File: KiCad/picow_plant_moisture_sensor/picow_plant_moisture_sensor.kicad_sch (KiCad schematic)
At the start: 28 parts, among them J1 Conn_01x03, J10 Conn_01x03, J11 Conn_01x03, J12 Conn_01x03, J13 Conn_01x03, J14 ADS1115, J15 ADS1115, J16 ADS1115, J2 Conn_01x03, J3 Conn_01x03, J4 Conn_01x03, J5 Conn_01x03, J6 Conn_01x03, J7 Conn_02x03_Odd_Even, J8 Conn_01x03, J9 Conn_01x03, SW1 SW_Push, SW2 SW_Push, SW3 SW_Push, SW4 SW_Push, U2 PicoW

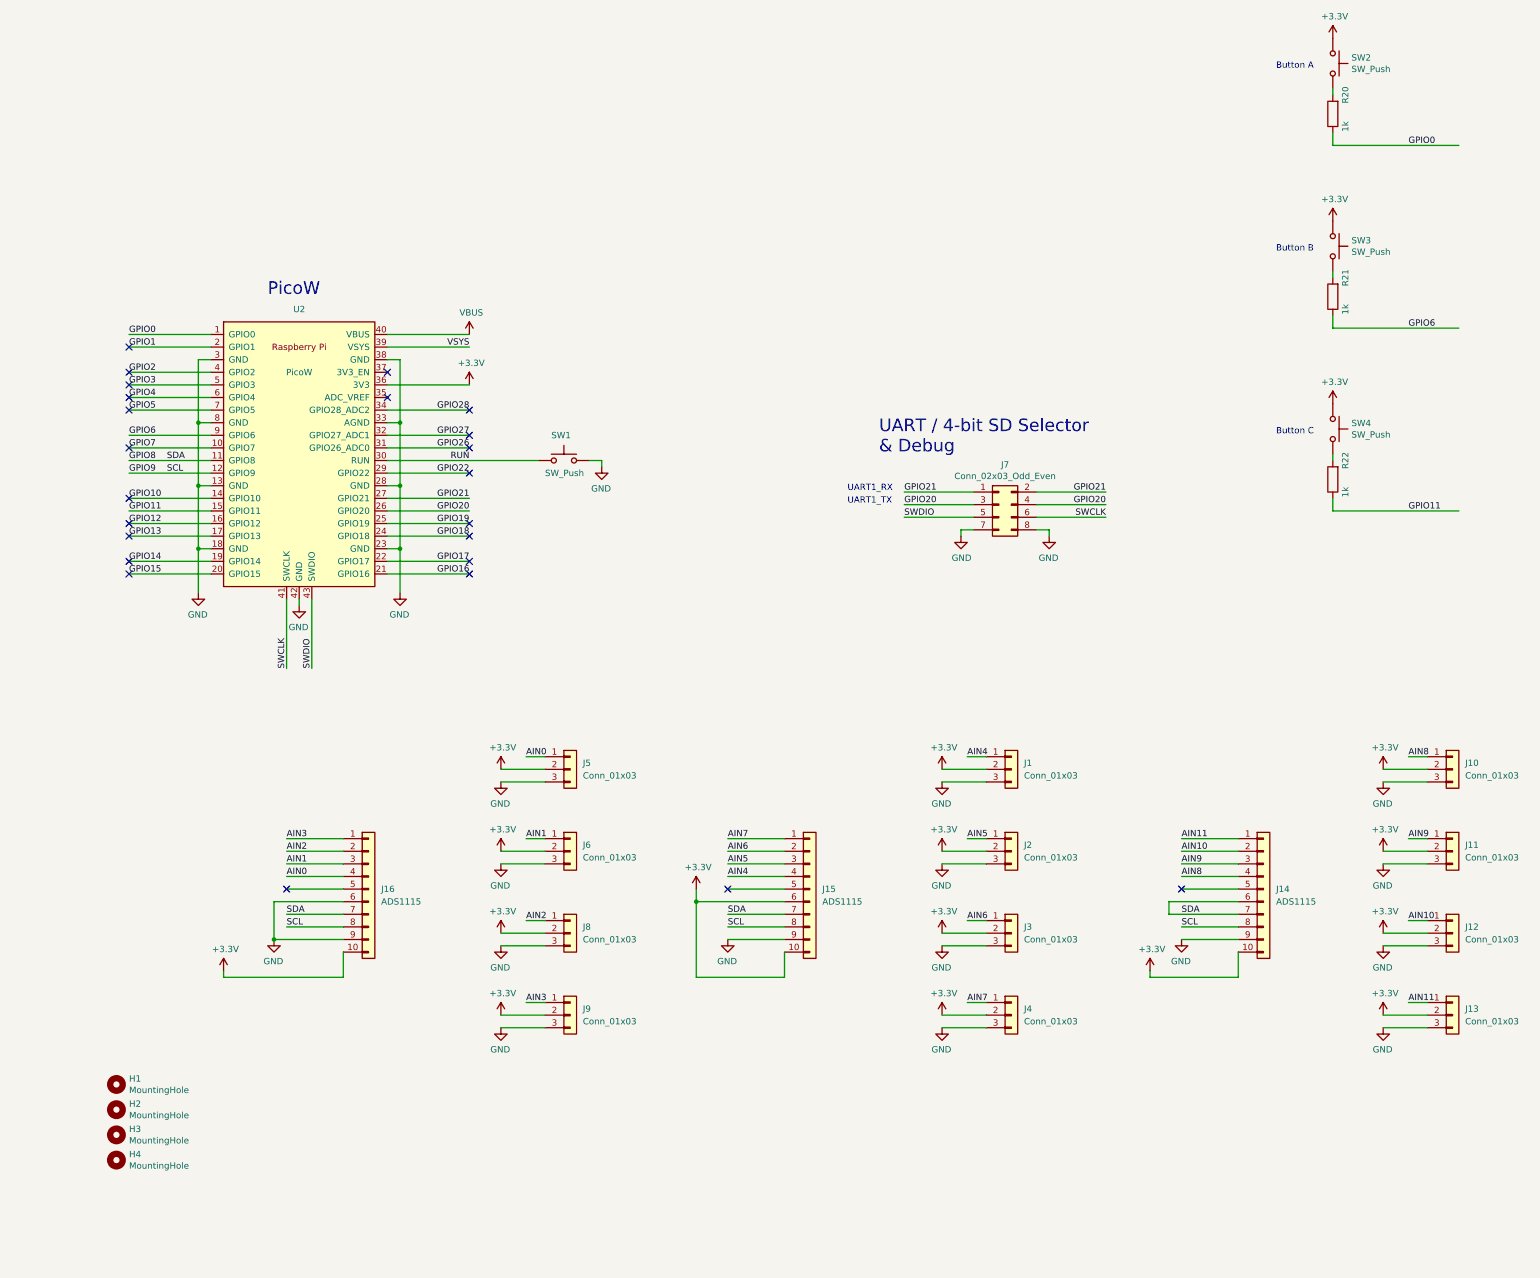
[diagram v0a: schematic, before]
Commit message: 10 pcb design with ics instead of complete pcb on headers (#11)
* No traces

* Routing done

* Complete PCB design with component references

* Rev1 ordered
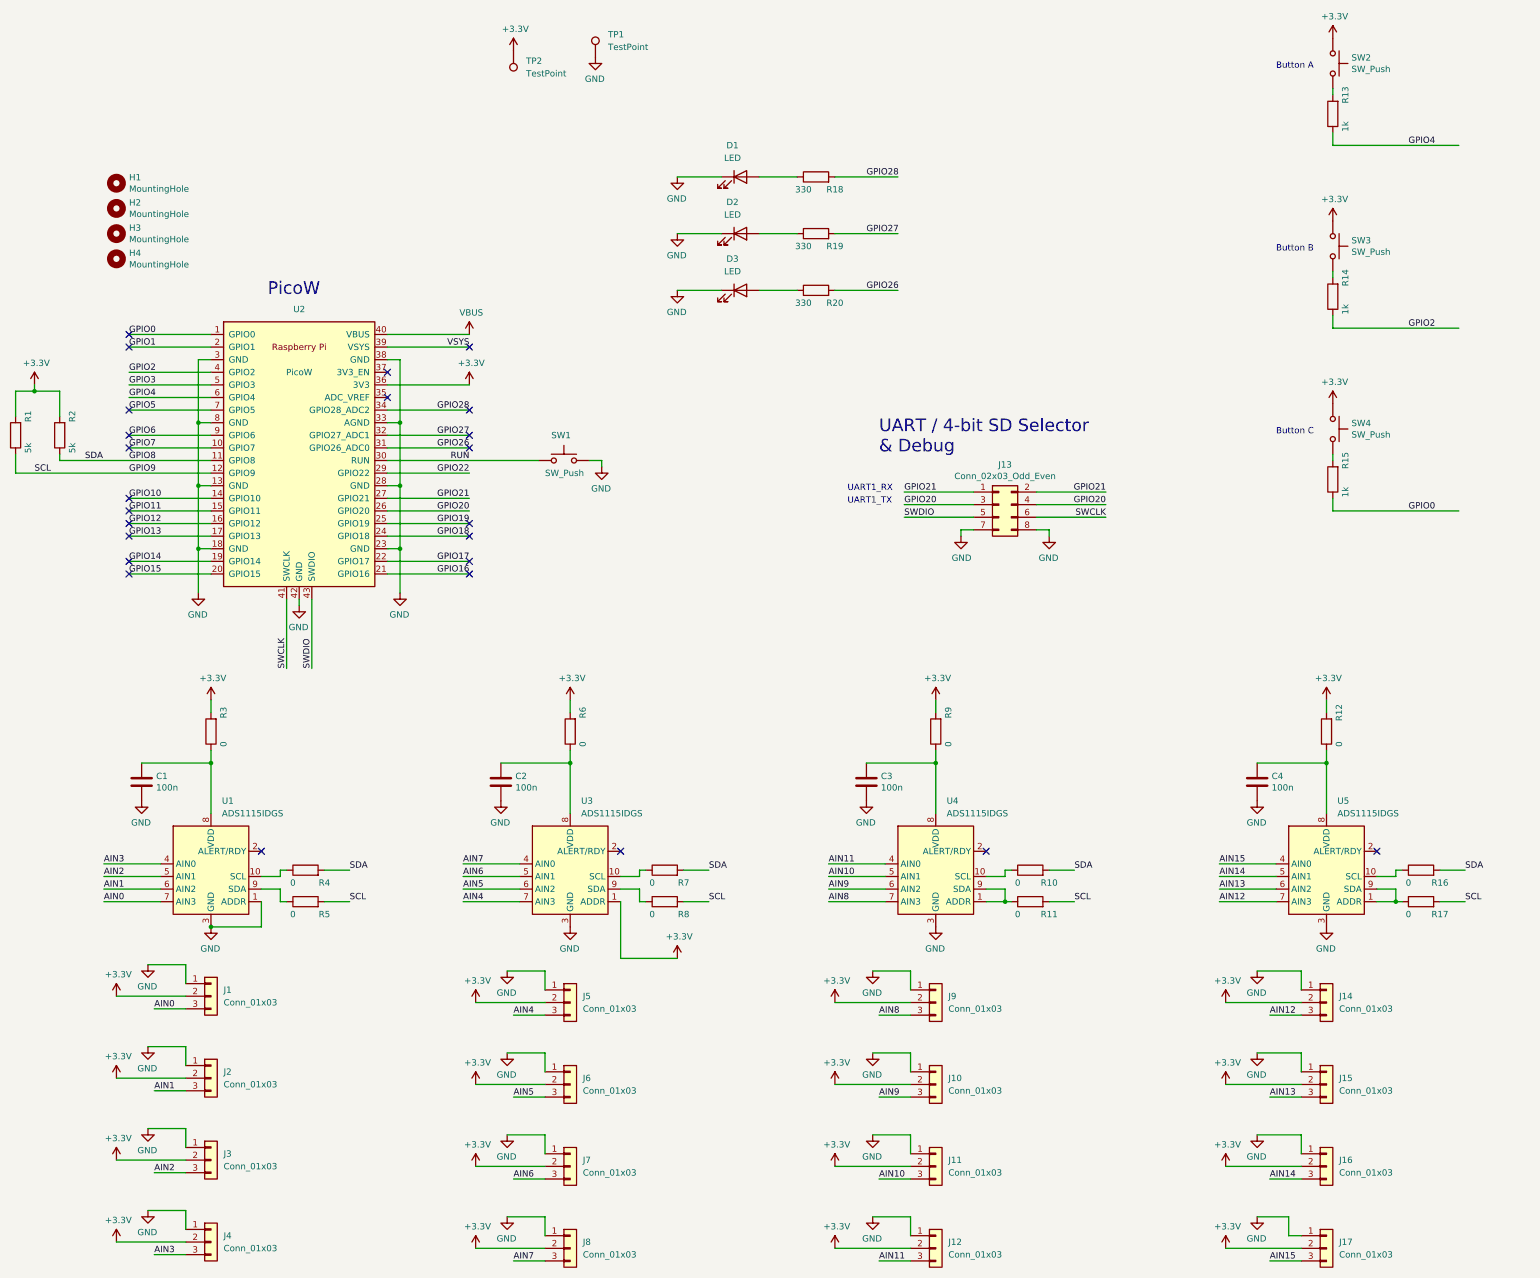
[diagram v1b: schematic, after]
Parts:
- removed J14, J15, J16: ADS1115, Connector_PinHeader_2.54mm:PinHeader_1x10_P2.54mm_Vertical, symbol Connector_Generic:Conn_01x10
- added C1, C2, C3, C4: 100n, Capacitor_SMD:C_0402_1005Metric, symbol Device:C
- added D1, D2, D3: LED, LED_SMD:LED_0603_1608Metric, symbol Device:LED
- added J14, J15, J16, J17: Conn_01x03, Connector_JST:JST_PH_B3B-PH-K_1x03_P2.00mm_Vertical, symbol Connector_Generic:Conn_01x03
- added R1, R2: 5k, Resistor_SMD:R_0402_1005Metric, symbol Device:R
- added R10, R11, R12, R16, R17, R3, R4, R5, R6, R7, R8, R9: 0, Resistor_SMD:R_0603_1608Metric, symbol Device:R
- added R18, R19, R20: 330, Resistor_SMD:R_0402_1005Metric, symbol Device:R
- added TP1, TP2: TestPoint, TestPoint:TestPoint_Pad_D2.0mm, symbol Connector:TestPoint
- added U1, U3, U4, U5: ADS1115IDGS, Package_SO:TSSOP-10_3x3mm_P0.5mm, symbol Analog_ADC:ADS1115IDGS
- J1: renamed from J5; footprint Connector_PinHeader_2.54mm:PinHeader_1x03_P2.54mm_Vertical -> Connector_JST:JST_PH_B3B-PH-K_1x03_P2.00mm_Vertical
- J10: renamed from J11; footprint Connector_PinHeader_2.54mm:PinHeader_1x03_P2.54mm_Vertical -> Connector_JST:JST_PH_B3B-PH-K_1x03_P2.00mm_Vertical
- J11: renamed from J12; footprint Connector_PinHeader_2.54mm:PinHeader_1x03_P2.54mm_Vertical -> Connector_JST:JST_PH_B3B-PH-K_1x03_P2.00mm_Vertical
- J12: renamed from J13; footprint Connector_PinHeader_2.54mm:PinHeader_1x03_P2.54mm_Vertical -> Connector_JST:JST_PH_B3B-PH-K_1x03_P2.00mm_Vertical
- J2: renamed from J6; footprint Connector_PinHeader_2.54mm:PinHeader_1x03_P2.54mm_Vertical -> Connector_JST:JST_PH_B3B-PH-K_1x03_P2.00mm_Vertical
- J3: renamed from J8; footprint Connector_PinHeader_2.54mm:PinHeader_1x03_P2.54mm_Vertical -> Connector_JST:JST_PH_B3B-PH-K_1x03_P2.00mm_Vertical
- J4: renamed from J9; footprint Connector_PinHeader_2.54mm:PinHeader_1x03_P2.54mm_Vertical -> Connector_JST:JST_PH_B3B-PH-K_1x03_P2.00mm_Vertical
- J5: renamed from J1; footprint Connector_PinHeader_2.54mm:PinHeader_1x03_P2.54mm_Vertical -> Connector_JST:JST_PH_B3B-PH-K_1x03_P2.00mm_Vertical
- J6: renamed from J2; footprint Connector_PinHeader_2.54mm:PinHeader_1x03_P2.54mm_Vertical -> Connector_JST:JST_PH_B3B-PH-K_1x03_P2.00mm_Vertical
- J7: renamed from J3; footprint Connector_PinHeader_2.54mm:PinHeader_1x03_P2.54mm_Vertical -> Connector_JST:JST_PH_B3B-PH-K_1x03_P2.00mm_Vertical
- J8: renamed from J4; footprint Connector_PinHeader_2.54mm:PinHeader_1x03_P2.54mm_Vertical -> Connector_JST:JST_PH_B3B-PH-K_1x03_P2.00mm_Vertical
- J9: renamed from J10; footprint Connector_PinHeader_2.54mm:PinHeader_1x03_P2.54mm_Vertical -> Connector_JST:JST_PH_B3B-PH-K_1x03_P2.00mm_Vertical
- R13: renamed from R20; LCSC (none) -> C11702
- R14: renamed from R21; LCSC (none) -> C11702
- R15: renamed from R22; LCSC (none) -> C11702
- SW1, SW2, SW3, SW4: footprint Button_Switch_SMD:SW_Push_1P1T_NO_Vertical_Wuerth_434133025816 -> Button_Switch_THT:SW_PUSH_6mm
- renumbered J7 to J13
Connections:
- net +3V3: now also J14.2 (Pin_2), J15.2 (Pin_2), J16.2 (Pin_2), J17.2 (Pin_2), R1.2, R12.2, R2.2, R3.2, R6.2, R9.2, TP2.1, U3.1 (ADDR)
- net AIN0: now also J1.3 (Pin_3), U1.7 (AIN3); no longer J1.1 (Pin_1)
- net AIN1: now also J2.3 (Pin_3), U1.6 (AIN2); no longer J2.1 (Pin_1)
- net AIN10: now also J11.3 (Pin_3), U4.5 (AIN1); no longer J11.1 (Pin_1)
- net AIN11: now also J12.3 (Pin_3), U4.4 (AIN0); no longer J12.1 (Pin_1)
- net AIN2: now also J3.3 (Pin_3), U1.5 (AIN1); no longer J3.1 (Pin_1)
- net AIN3: now also J4.3 (Pin_3), U1.4 (AIN0); no longer J4.1 (Pin_1)
- net AIN4: now also J5.3 (Pin_3), U3.7 (AIN3); no longer J5.1 (Pin_1)
- net AIN5: now also J6.3 (Pin_3), U3.6 (AIN2); no longer J6.1 (Pin_1)
- net AIN6: now also J7.3 (Pin_3), U3.5 (AIN1); no longer J7.1 (Pin_1)
- net AIN7: now also J8.3 (Pin_3), U3.4 (AIN0); no longer J8.1 (Pin_1)
- net AIN8: now also J9.3 (Pin_3), U4.7 (AIN3); no longer J9.1 (Pin_1)
- net AIN9: now also J10.3 (Pin_3), U4.6 (AIN2); no longer J10.1 (Pin_1)
- net GND: now also J1.1 (Pin_1), J10.1 (Pin_1), J11.1 (Pin_1), J12.1 (Pin_1), J2.1 (Pin_1), J3.1 (Pin_1), J4.1 (Pin_1), J5.1 (Pin_1), J6.1 (Pin_1), J7.1 (Pin_1), J8.1 (Pin_1), J9.1 (Pin_1), C1.2, C2.2, C3.2, C4.2, D1.1 (K), D2.1 (K), D3.1 (K), J14.1 (Pin_1), J15.1 (Pin_1), J16.1 (Pin_1), J17.1 (Pin_1), TP1.1, U1.1 (ADDR), U1.3 (GND), U3.3 (GND), U4.3 (GND), U5.3 (GND); no longer J1.3 (Pin_3), J10.3 (Pin_3), J11.3 (Pin_3), J12.3 (Pin_3), J2.3 (Pin_3), J3.3 (Pin_3), J4.3 (Pin_3), J5.3 (Pin_3), J6.3 (Pin_3), J7.3 (Pin_3), J8.3 (Pin_3), J9.3 (Pin_3)
- net GPIO0: now also R15.1; no longer R13.1
- net GPIO11: no longer R15.1
- net GPIO2: now also R14.1
- net GPIO26: now also R20.2
- net GPIO27: now also R19.2
- net GPIO28: now also R18.2
- net GPIO4: now also R13.1
- net GPIO6: no longer R14.1
- net GPIO8: now also R10.2, R16.2, R2.1, R4.2, R7.2
- net GPIO9: now also R1.1, R11.2, R17.2, R5.2, R8.2
- new net: C1.1, R3.1, U1.8 (VDD)
- new net: R10.1, U4.10 (SCL)
- new net: C4.1, R12.1, U5.8 (VDD)
- new net: C2.1, R6.1, U3.8 (VDD)
- new net: R4.1, U1.10 (SCL)
- new net: R5.1, U1.9 (SDA)
- new net: R16.1, U5.10 (SCL)
- new net: R17.1, U5.1 (ADDR), U5.9 (SDA)
- new net: D3.2 (A), R20.1
- new net: D2.2 (A), R19.1
- new net: R7.1, U3.10 (SCL)
- new net: R8.1, U3.9 (SDA)
- new net: C3.1, R9.1, U4.8 (VDD)
- new net: R11.1, U4.1 (ADDR), U4.9 (SDA)
- new net: D1.2 (A), R18.1
- new net AIN12: J14.3 (Pin_3), U5.7 (AIN3)
- new net AIN13: J15.3 (Pin_3), U5.6 (AIN2)
- new net AIN14: J16.3 (Pin_3), U5.5 (AIN1)
- new net AIN15: J17.3 (Pin_3), U5.4 (AIN0)
- no-connect marks 24 -> 25
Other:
- company: Raspberry Pi Ltd -> Andreas Andersson
- title: RPI-PWVSA    VGA, SD Card & Audio Demo Board for Pico W -> Analog Sensor Board for Pico W
- moved on the sheet: H1, H2, H3, H4, J1, J10, J11, J12, J2, J3, J4, J5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
